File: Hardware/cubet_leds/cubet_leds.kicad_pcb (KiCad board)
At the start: 2 copper layers, 50 x 50 mm, 139 parts, among them J1 Conn_01x01, J10 Conn_01x01, J11 Conn_01x01, J2 Conn_01x32, J3 Conn_01x32, J4 Conn_01x32, J5 Conn_01x01, J6 Conn_01x01, J7 Conn_01x01, J8 Conn_01x01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

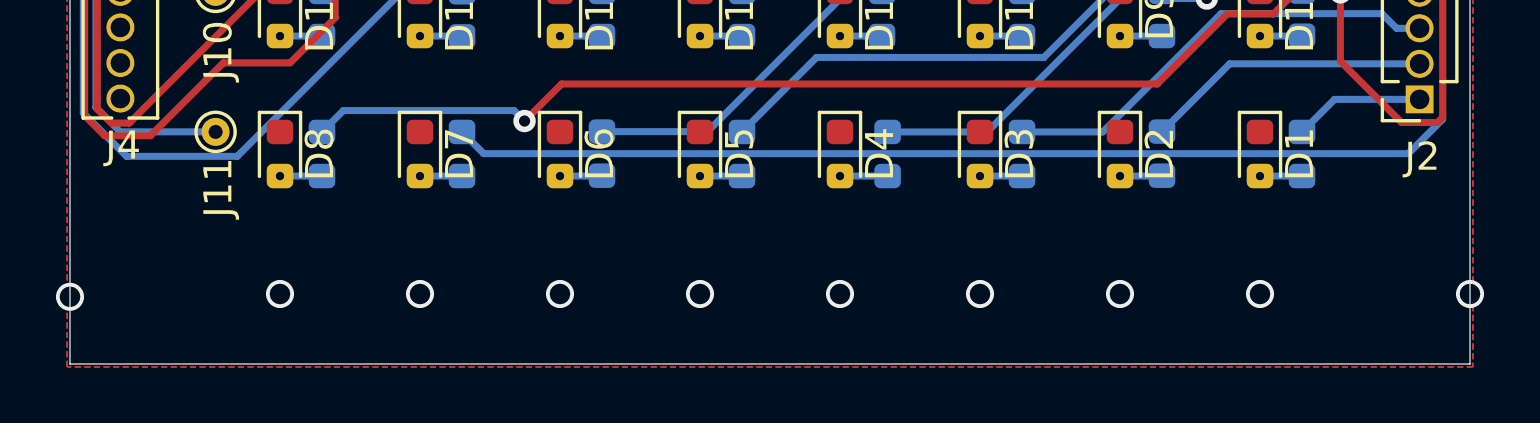
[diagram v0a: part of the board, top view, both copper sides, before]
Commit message: First working SPI. First work in README
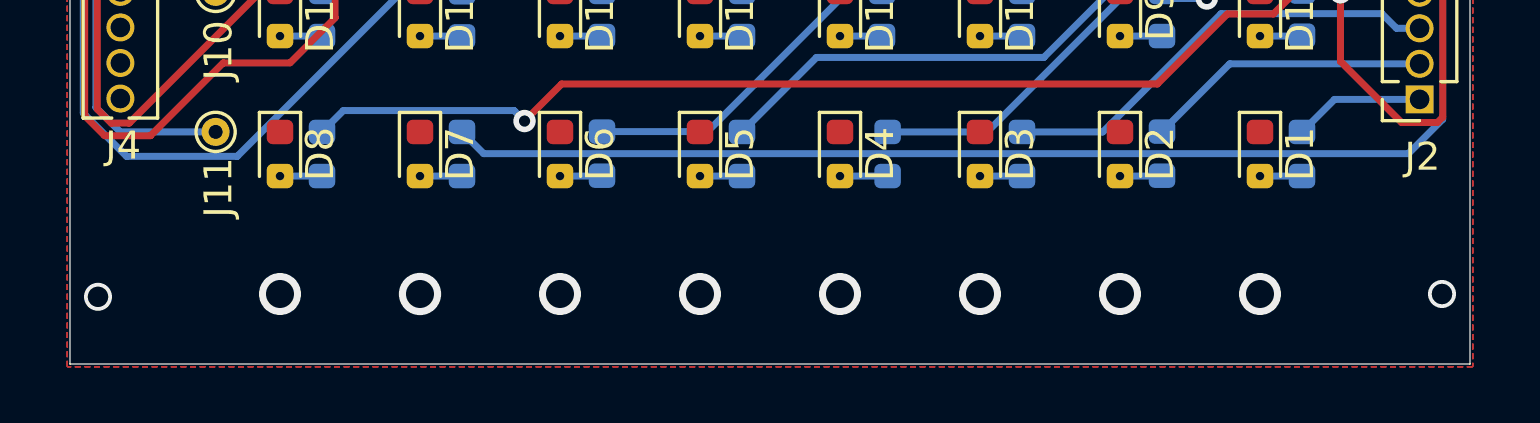
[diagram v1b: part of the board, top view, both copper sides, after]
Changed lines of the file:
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@@
   (gr_line (start 100 50) (end 50 50) (layer Edge.Cuts) (width 0.05))
   (gr_line (start 50 100) (end 100 100) (layer Edge.Cuts) (width 0.05))
-  (via (at 57.5 97.5) (size 1) (drill 0.73) (layers F.Cu B.Cu) (net 0))
-  (via (at 62.5 97.5) (size 1) (drill 0.73) (layers F.Cu B.Cu) (net 0))
-  (via (at 67.5 97.5) (size 1) (drill 0.73) (layers F.Cu B.Cu) (net 0))
-  (via (at 72.5 97.5) (size 1) (drill 0.73) (layers F.Cu B.Cu) (net 0))
-  (via (at 77.5 97.5) (size 1) (drill 0.73) (layers F.Cu B.Cu) (net 0))
-  (via (at 82.5 97.5) (size 1) (drill 0.73) (layers F.Cu B.Cu) (net 0))
-  (via (at 87.5 97.5) (size 1) (drill 0.73) (layers F.Cu B.Cu) (net 0))
-  (via (at 92.5 97.5) (size 1) (drill 0.73) (layers F.Cu B.Cu) (net 0))
-  (via (at 100 97.5) (size 1) (drill 0.73) (layers F.Cu B.Cu) (net 0))
-  (via (at 50 97.6) (size 1) (drill 0.73) (layers F.Cu B.Cu) (net 0))
+  (via (at 57.5 97.5) (size 1.5) (drill 1) (layers F.Cu B.Cu) (net 0))
+  (via (at 62.5 97.5) (size 1.51) (drill 1) (layers F.Cu B.Cu) (net 0))
+  (via (at 67.5 97.5) (size 1.5) (drill 1) (layers F.Cu B.Cu) (net 0))
+  (via (at 72.5 97.5) (size 1.5) (drill 1) (layers F.Cu B.Cu) (net 0))
+  (via (at 77.5 97.5) (size 1.5) (drill 1) (layers F.Cu B.Cu) (net 0))
+  (via (at 82.5 97.5) (size 1.5) (drill 1) (layers F.Cu B.Cu) (net 0))
+  (via (at 87.5 97.5) (size 1.5) (drill 1) (layers F.Cu B.Cu) (net 0))
+  (via (at 92.5 97.5) (size 1.5) (drill 1) (layers F.Cu B.Cu) (net 0))
+  (via (at 99 97.5) (size 1) (drill 0.73) (layers F.Cu B.Cu) (net 0))
+  (via (at 51 97.6) (size 1) (drill 0.73) (layers F.Cu B.Cu) (net 0))
   (segment (start 55.2 56.71) (end 54.5268 56.71) (width 0.25) (layer B.Cu) (net 2))
   (segment (start 54.5268 56.71) (end 53.4594 57.7774) (width 0.25) (layer B.Cu) (net 2))
